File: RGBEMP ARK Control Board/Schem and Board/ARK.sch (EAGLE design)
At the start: 5 parts, among them IC1 LM1117MP-3.3, U1 ESP-WROOM-02

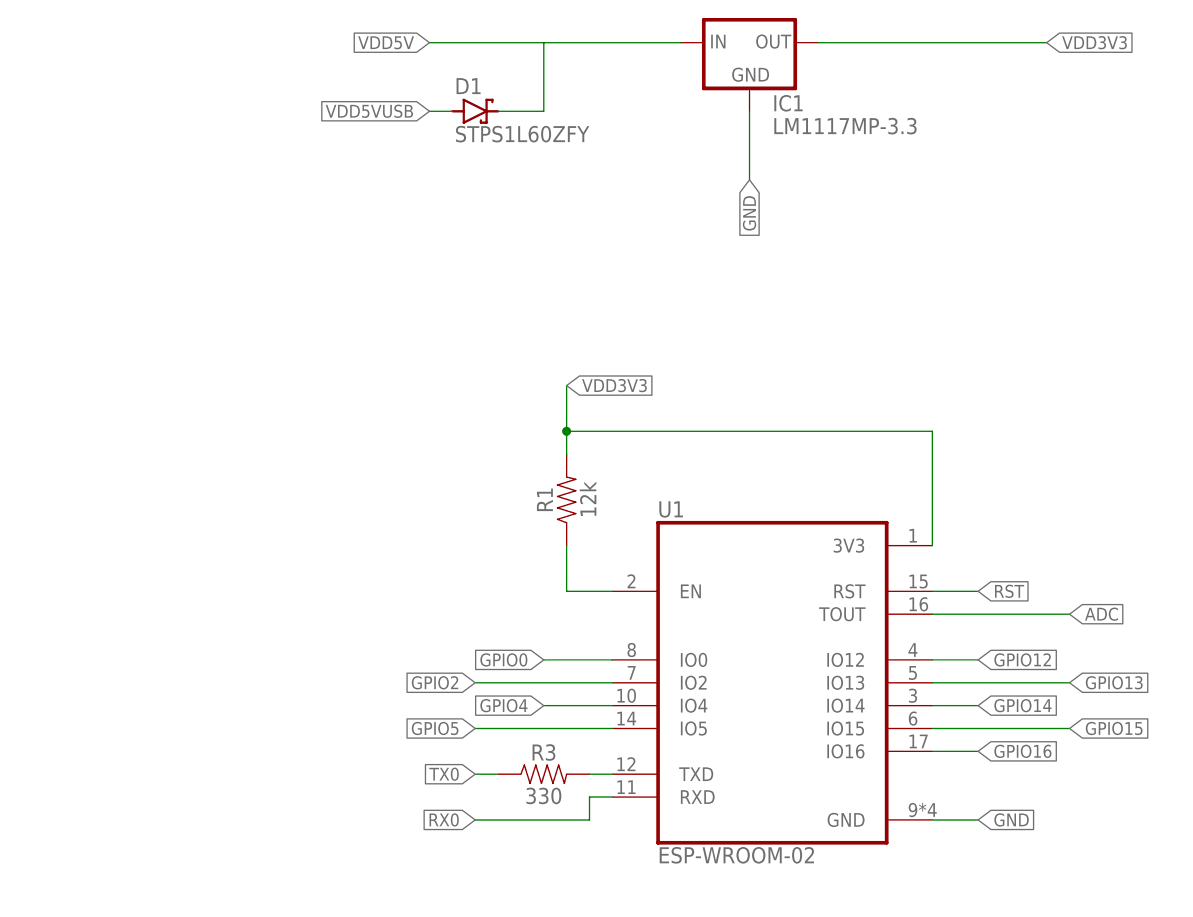
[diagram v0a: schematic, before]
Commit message: Adding esp32 and other stuff
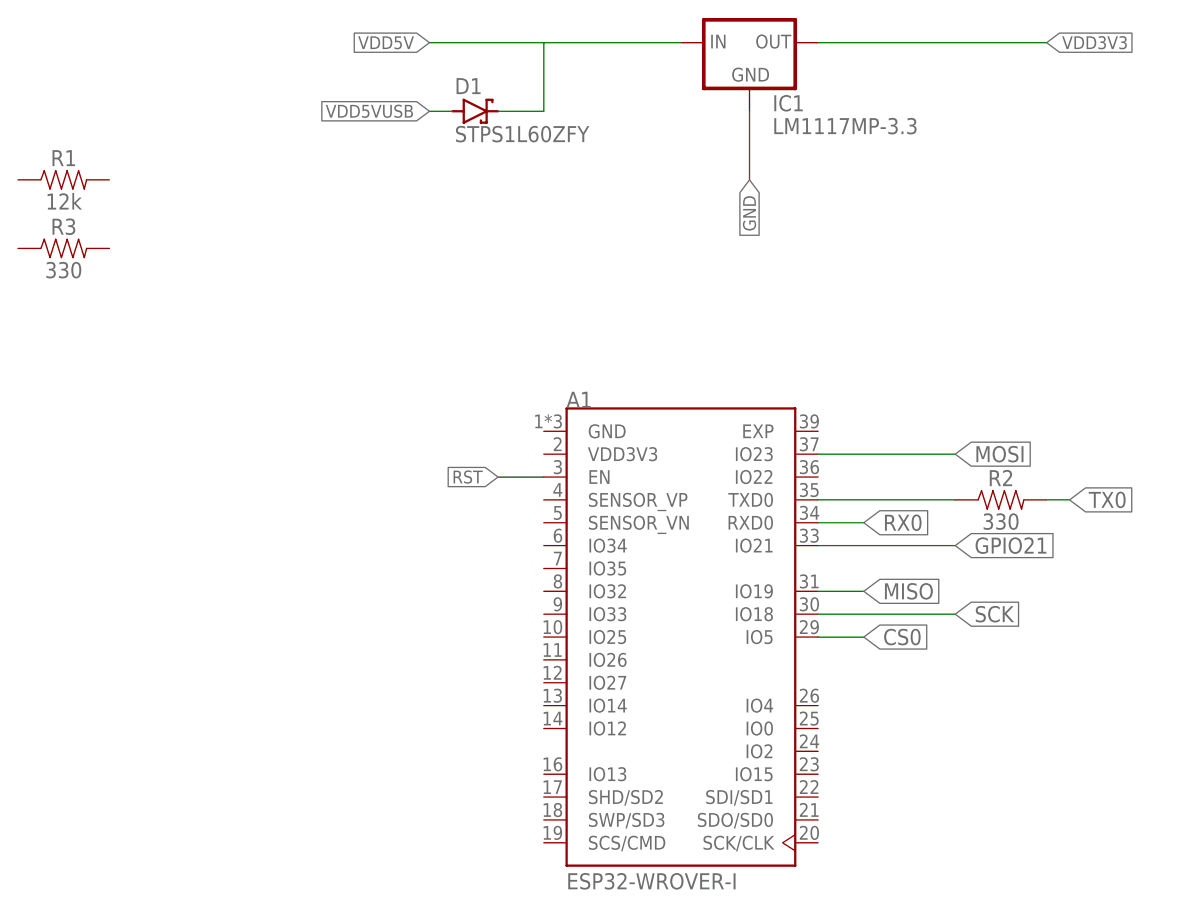
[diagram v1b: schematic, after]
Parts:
- removed U1: ESP-WROOM-02, ESP-WROOM-02:ESP-WROOM-02
- added A1: ESP32-WROVER-I, ESP32-WROVER-I:ESP32-WROVER-I
- added R2: 330, SparkFun-Resistors:12KOHM-0603-1/10W-1%
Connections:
- removed net ADC: U1.TOUT
- removed net GPIO0: U1.IO0
- removed net GPIO12: U1.IO12
- removed net GPIO13: U1.IO13
- removed net GPIO14: U1.IO14
- removed net GPIO15: U1.IO15
- removed net GPIO16: U1.IO16
- removed net GPIO2: U1.IO2
- removed net GPIO4: U1.IO4
- removed net GPIO5: U1.IO5
- removed net N$2: R3.2, U1.TXD
- new net CS0: A1.IO5
- new net GPIO21: A1.IO21
- new net MISO: A1.IO19
- new net MOSI: A1.IO23
- new net SCK: A1.IO18
- net GND: no longer U1.GND
- net N$1: now also A1.TXD0, R2.1; no longer R1.1, U1.EN
- net RST: now also A1.EN; no longer U1.RST
- net RX0: now also A1.RXD0; no longer U1.RXD
- net TX0: now also R2.2; no longer R3.1
- net VDD3V3: no longer R1.2, U1.3V3
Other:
- moved on the sheet: R1, R3
